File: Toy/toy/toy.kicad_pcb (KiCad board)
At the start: 2 copper layers, 190 x 119.5 mm, 25 parts, among them J1 Conn_01x07_Pin, J2 Conn_01x03_Pin, J3 Conn_01x03_Pin, J4 Conn_01x03_Pin

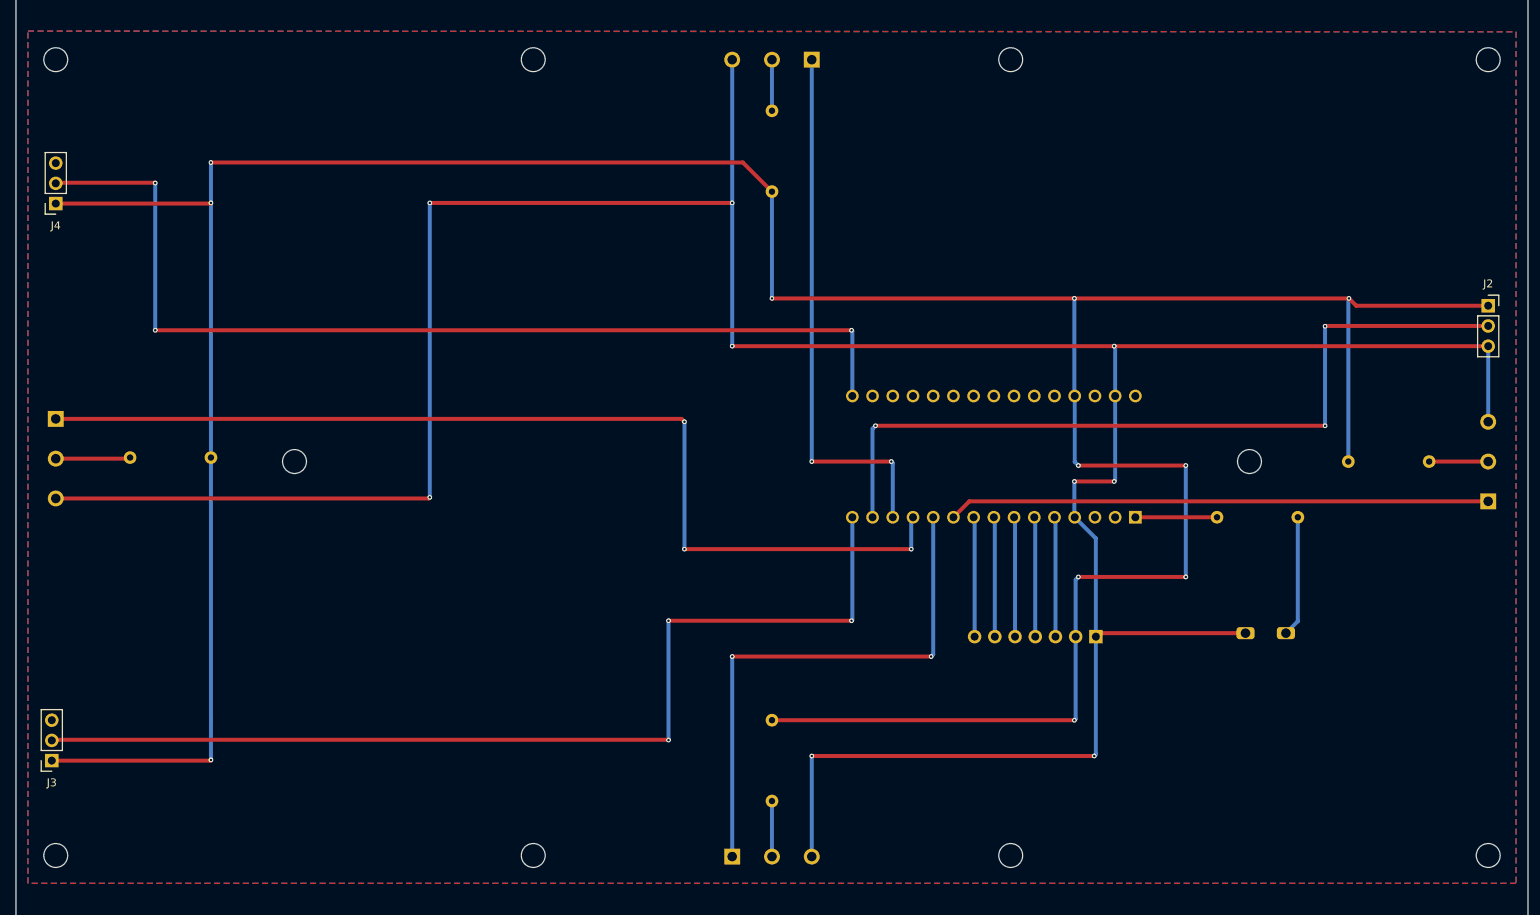
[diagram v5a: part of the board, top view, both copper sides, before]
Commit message: PCB updates, change switches to SPST style
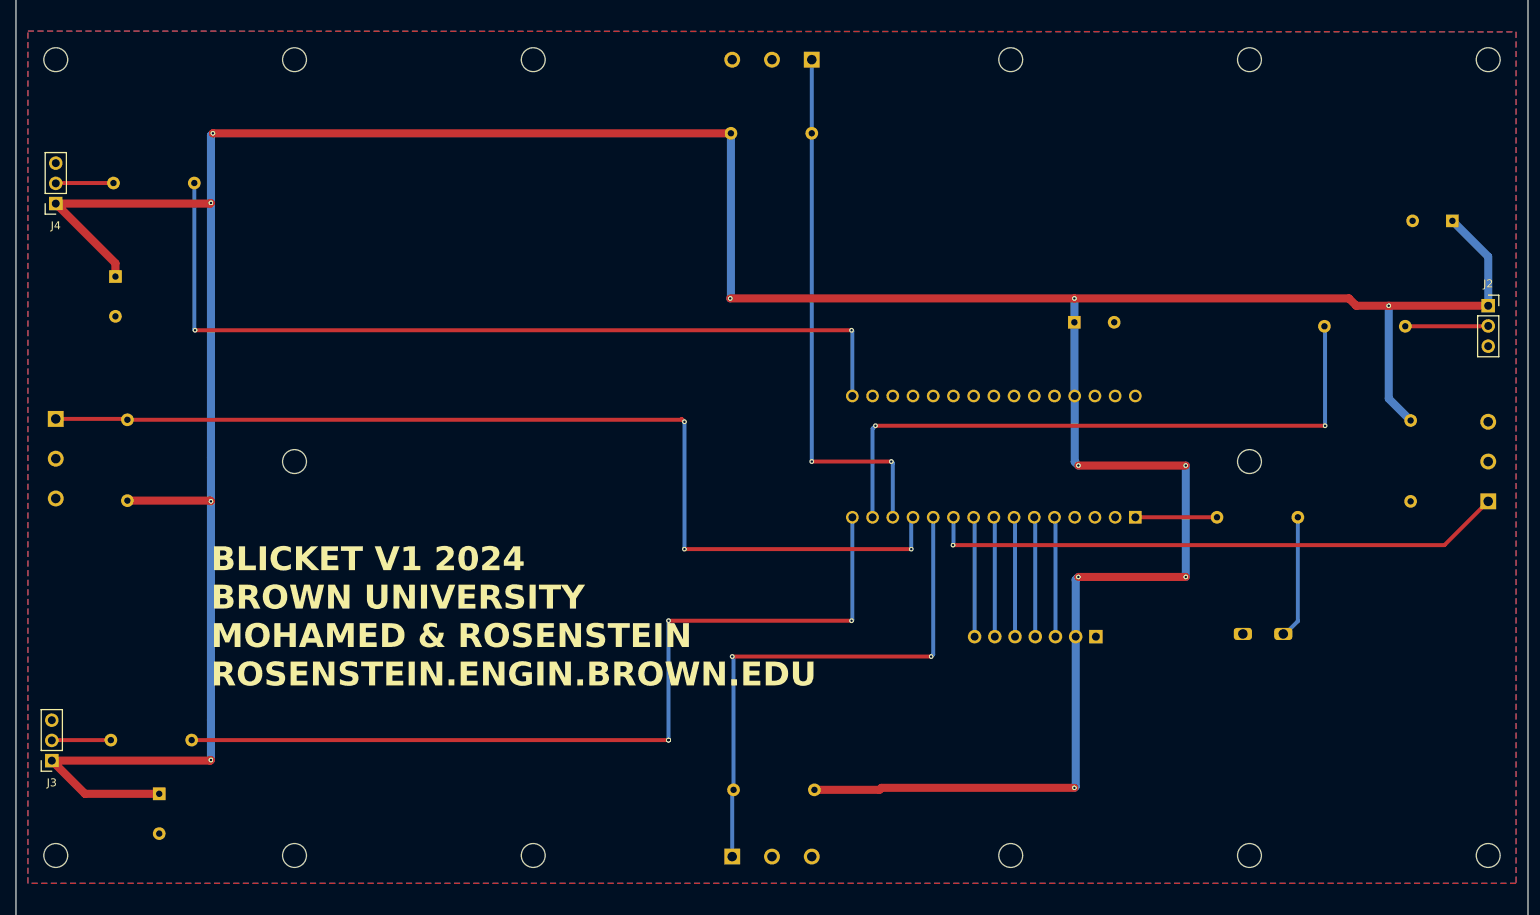
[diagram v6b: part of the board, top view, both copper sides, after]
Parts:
- added C1: C_Polarized, Capacitor_THT:CP_Radial_Tantal_D5.5mm_P5.00mm, B.Cu at (54.0, 68.2)
- added C2: C_Polarized, Capacitor_THT:CP_Radial_Tantal_D5.5mm_P5.00mm, B.Cu at (59.5, 133.2)
- added C3: C_Polarized, Capacitor_THT:CP_Radial_Tantal_D5.5mm_P5.00mm, B.Cu at (174.5, 74.0)
- added C4: C_Polarized, Capacitor_THT:CP_Radial_Tantal_D5.5mm_P5.00mm, B.Cu at (222.0, 61.2)
- added R6: 10k, Resistor_THT:R_Axial_DIN0207_L6.3mm_D2.5mm_P10.16mm_Horizontal, B.Cu at (205.9, 74.5)
- added R7: 10k, Resistor_THT:R_Axial_DIN0207_L6.3mm_D2.5mm_P10.16mm_Horizontal, B.Cu at (63.6, 126.5)
- added R8: 10k, Resistor_THT:R_Axial_DIN0207_L6.3mm_D2.5mm_P10.16mm_Horizontal, B.Cu at (63.9, 56.5)
- added REF**: MountingHole_3mm, MountingHole:MountingHole_3mm, F.Cu at (76.5, 41.0)
- added REF**: MountingHole_3mm, MountingHole:MountingHole_3mm, F.Cu at (196.5, 41.0)
- added REF**: MountingHole_3mm, MountingHole:MountingHole_3mm, F.Cu at (196.5, 141.0)
- added REF**: MountingHole_3mm, MountingHole:MountingHole_3mm, F.Cu at (76.5, 141.0)
- moved R2 11.5 mm to (55.5, 86.2), turned to -90 degrees
- moved R3 9.99 mm to (131.7, 132.8), turned to 0 degrees
- moved R1 9.29 mm to (216.8, 96.5), turned to 90 degrees
- moved R4 8.87 mm to (141.5, 50.2), turned to 180 degrees
- moved U5 0.34 mm to (198.2, 103.0)
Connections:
- J2 pad 2: /LED1_ctrl -> Net-(J2-Pin_2)
- J3 pad 2: /LED2_ctrl -> Net-(J3-Pin_2)
- J4 pad 2: /LED3_ctrl -> Net-(J4-Pin_2)
- R1 pad 1: VDD -> /C_sw1
- R1 pad 2: Net-(U1-NO) -> VDD
- R2 pad 1: VDD -> /C_sw3
- R2 pad 2: Net-(U2-NO) -> VDD
- R3 pad 1: VDD -> /C_sw2
- R3 pad 2: Net-(U3-NO) -> VDD
- R4 pad 1: VDD -> /C_sw4
- R4 pad 2: Net-(U4-NO) -> VDD
- U1 pad 2: Net-(U1-NO) -> GND
- U1 pad 3: GND -> unconnected-(U1-NC-Pad3)
- U2 pad 2: Net-(U2-NO) -> GND
- U2 pad 3: GND -> unconnected-(U2-NC-Pad3)
- U3 pad 2: Net-(U3-NO) -> GND
- U3 pad 3: GND -> unconnected-(U3-NC-Pad3)
- U4 pad 2: Net-(U4-NO) -> GND
- U4 pad 3: GND -> unconnected-(U4-NC-Pad3)
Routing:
- net GND: track 388.3 -> 0.00 mm, vias 9 -> 0
- net VDD: track 429.4 -> 487.8 mm, vias 11 -> 12
- net /LED1_ctrl: track 101.2 -> 80.6 mm, vias 3 -> 2
- net /LED3_ctrl: track 126.8 -> 109.3 mm, vias 3 -> 2
- net /LED2_ctrl: track 128.1 -> 111.0 mm, vias 3 -> 4
- net Net-(J2-Pin_2): track 0.00 -> 10.4 mm
- net Net-(U2-NO): track 9.53 -> 0.00 mm
- net Net-(J3-Pin_2): track 0.00 -> 7.44 mm
- net Net-(U1-NO): track 7.42 -> 0.00 mm
- net Net-(U3-NO): track 7.34 -> 0.00 mm
- net Net-(J4-Pin_2): track 0.00 -> 7.27 mm
- net Net-(U4-NO): track 5.92 -> 0.00 mm
- net /C_sw1: track 68.0 -> 73.0 mm, vias 0 -> 1
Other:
- board text added: "BLICKET V1 2024 BROWN UNIVERSITY MOHAMED & ROSENSTEIN ROSENSTEIN.ENGIN.BROWN.EDU"

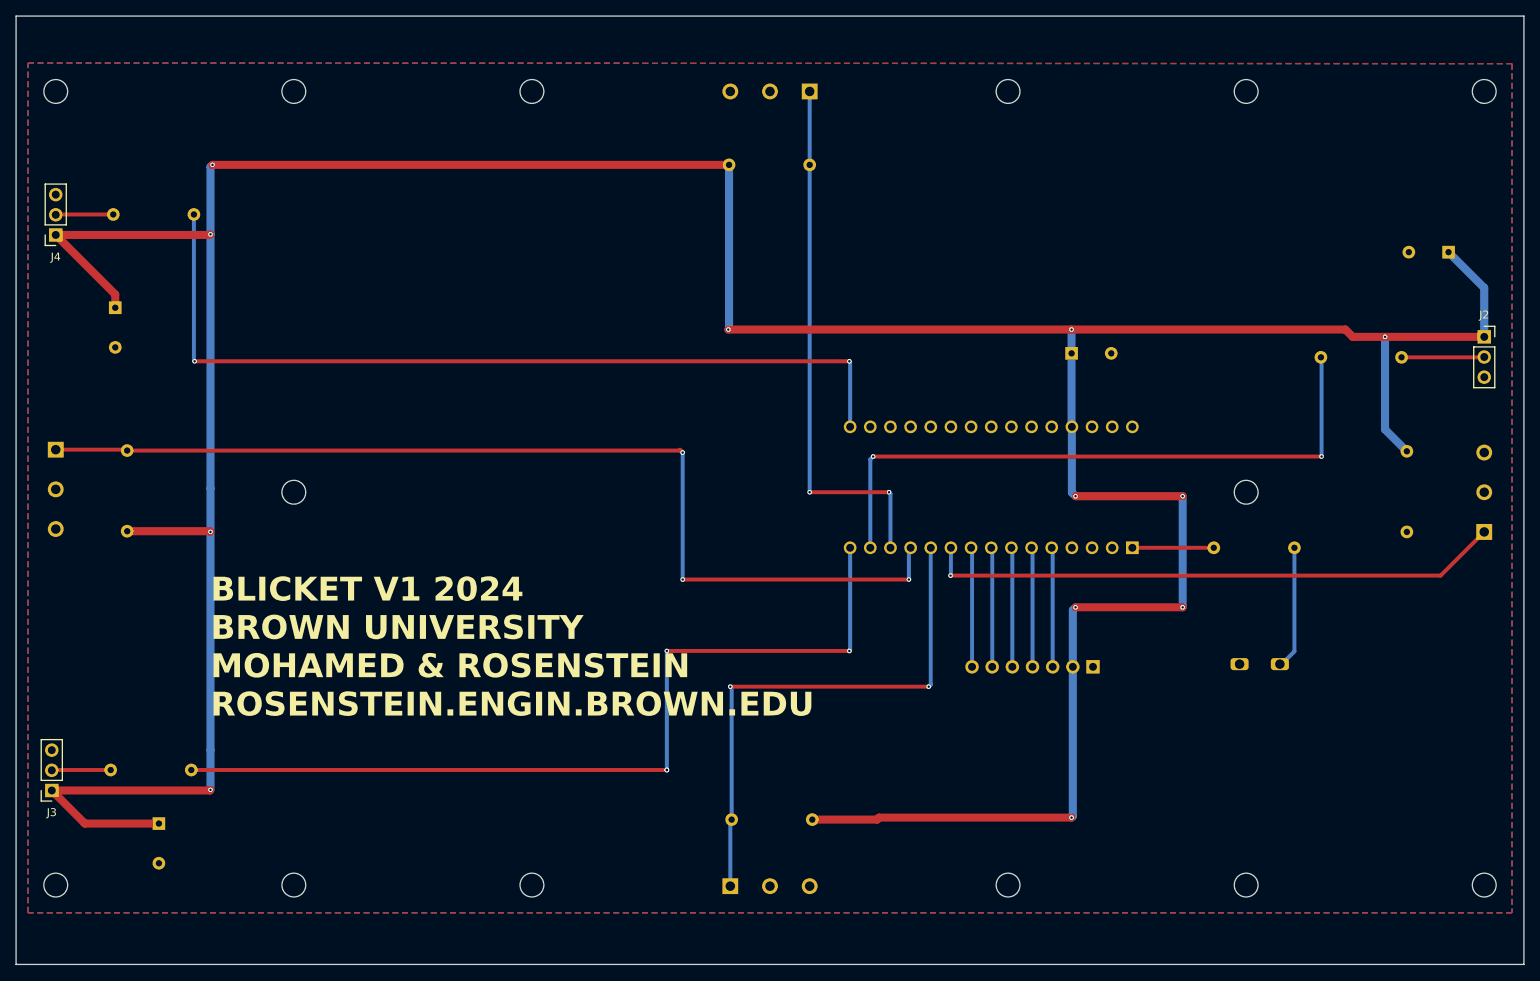
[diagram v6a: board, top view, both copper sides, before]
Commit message: PCB updates, move LEDs to same side; 6 switches; move standoff holes to edges
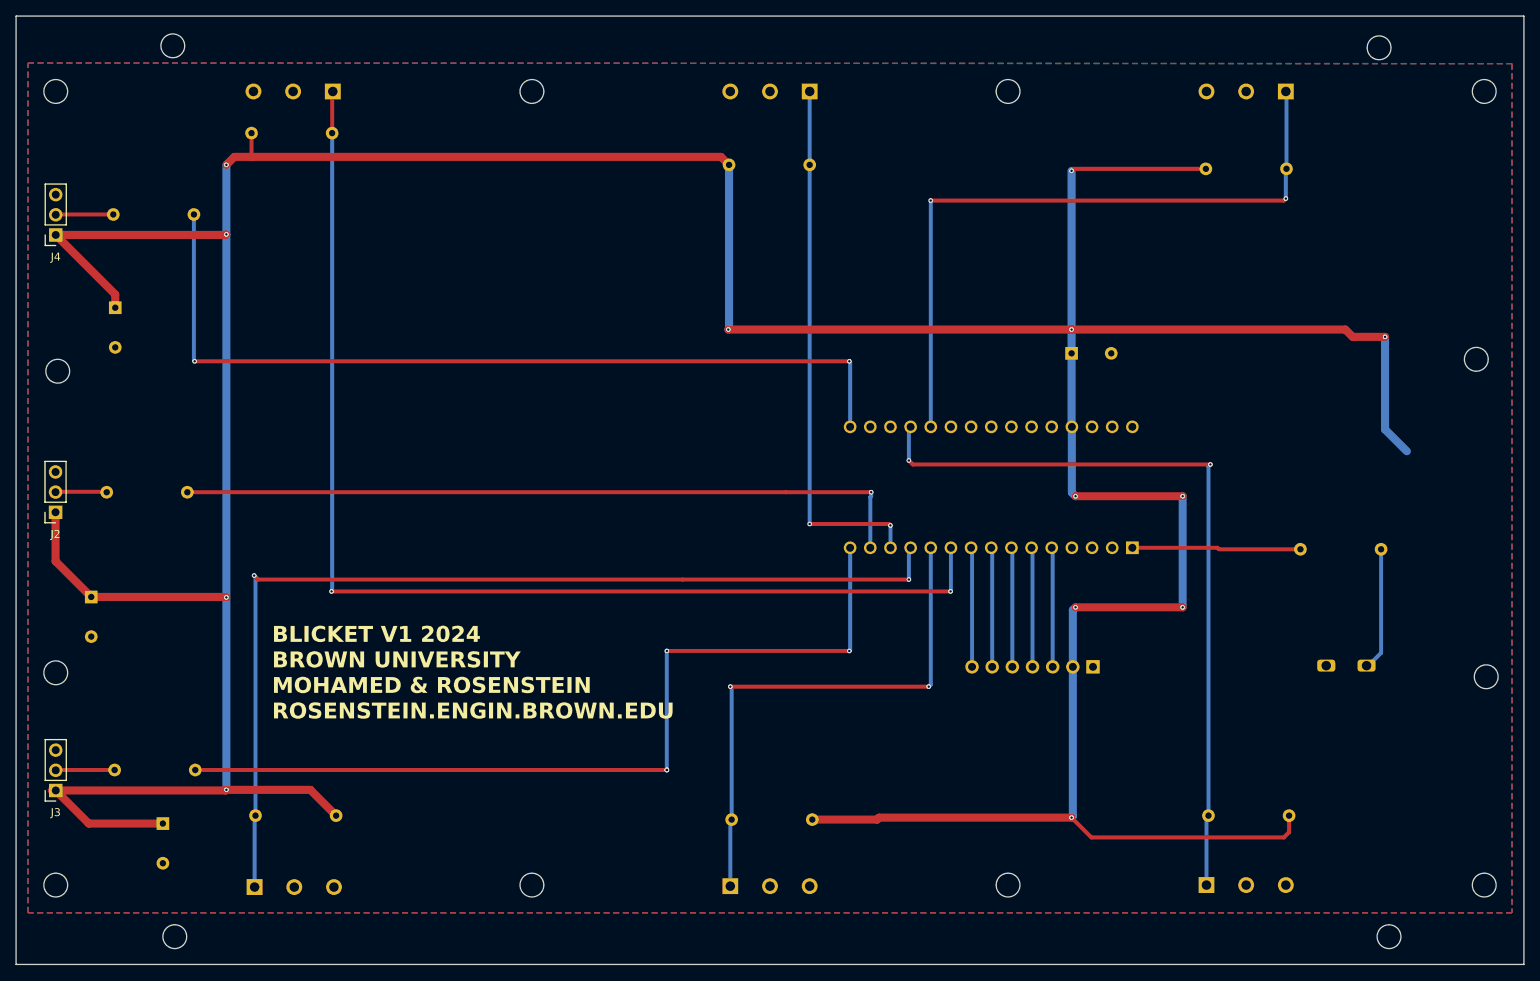
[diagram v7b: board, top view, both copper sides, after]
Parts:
- removed the REF** at (196.5, 91.5)
- removed the REF** at (76.5, 91.5)
- added R10: 10k, Resistor_THT:R_Axial_DIN0207_L6.3mm_D2.5mm_P10.16mm_Horizontal, B.Cu at (201.6, 50.8)
- added R9: 10k, Resistor_THT:R_Axial_DIN0207_L6.3mm_D2.5mm_P10.16mm_Horizontal, B.Cu at (191.8, 132.2)
- added REF**: MountingHole_3mm, MountingHole:MountingHole_3mm, F.Cu at (46.8, 76.2)
- added REF**: MountingHole_3mm, MountingHole:MountingHole_3mm, F.Cu at (226.8, 114.8)
- added REF**: MountingHole_3mm, MountingHole:MountingHole_3mm, F.Cu at (225.5, 74.8)
- added REF**: MountingHole_3mm, MountingHole:MountingHole_3mm, F.Cu at (46.5, 114.2)
- added U6: ~, First_cost_Library:switch, F.Cu at (204.5, 146.0)
- added U7: ~, First_cost_Library:switch, F.Cu at (188.5, 36.0)
- moved J2 181.4 mm to (46.5, 94.0), turned to 180 degrees
- moved C4 176.5 mm to (51.0, 104.7), turned to -90 degrees
- moved U1 169.9 mm to (68.4, 36.0), turned to -90 degrees
- moved R1 144.4 mm to (81.3, 46.2), turned to 180 degrees
- moved R6 143.8 mm to (63.1, 91.5), turned to 180 degrees
- moved U2 63.8 mm to (84.6, 146.2), turned to 90 degrees
- moved R2 48.8 mm to (71.7, 132.2), turned to 0 degrees
- moved REF** 19.1 mm to (214.5, 147.5)
- moved REF** 17.6 mm to (213.2, 35.5)
- moved REF** 16.3 mm to (61.5, 147.5)
- moved REF** 16.3 mm to (61.2, 35.2)
- moved R5 10.9 mm to (213.5, 98.7)
- moved U5 10.9 mm to (209.1, 103.2)
- moved C2 0.50 mm to (60.0, 133.2)
- moved J3 0.50 mm to (46.5, 129.1)
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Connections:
- A1 pad 19: unconnected-(A1-A0-Pad19) -> /C_sw5
- A1 pad 20: unconnected-(A1-A1-Pad20) -> /C_sw6
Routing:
- net /C_sw5: track 0.00 -> 95.7 mm, vias 0 -> 2
- net /C_sw6: track 0.00 -> 86.9 mm, vias 0 -> 2
- net VDD: track 487.8 -> 570.8 mm, vias 12 -> 13
- net /C_sw1: track 73.0 -> 146.6 mm, vias 1 -> 2
- net /LED1_ctrl: track 80.6 -> 93.2 mm, vias 2 -> 1
- net /BUZZ: track 10.3 -> 21.3 mm
- net Net-(J2-Pin_2): track 10.4 -> 6.43 mm
- net /C_sw3: track 128.3 -> 126.2 mm, vias 3 -> 2
